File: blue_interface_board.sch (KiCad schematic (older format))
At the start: 0 parts

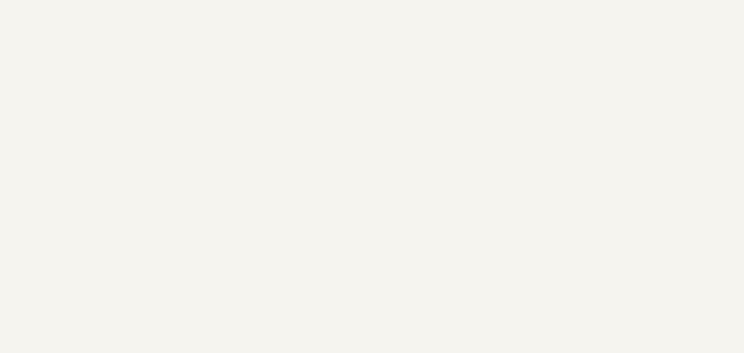
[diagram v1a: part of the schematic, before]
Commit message: Finished schematic, placement and routing, only silkscreen TODO
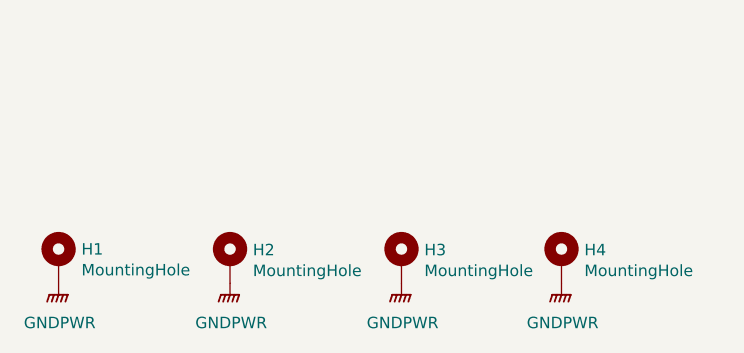
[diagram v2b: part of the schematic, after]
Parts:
- added H1, H2, H3, H4: MountingHole, MountingHole:MountingHole_2.5mm_Pad_Via, symbol Mechanical:MountingHole_Pad
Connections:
- new net GNDPWR: H1.1, H2.1, H3.1, H4.1
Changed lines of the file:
@@
 EESchema Schematic File Version 5
 LIBS:blue_interface_board-cache
-EELAYER 29 0
+EELAYER 30 0
 EELAYER END
 $Descr A4 11693 8268
@@
 F1 "Power.sch" 50
 $EndSheet
+$Comp
+L Mechanical:MountingHole_Pad H1
+U 1 1 5D50B183
+P 750 4250
+F 0 "H1" H 850 4299 50  0000 L CNN
+F 1 "MountingHole" H 850 4208 50  0000 L CNN
+F 2 "MountingHole:MountingHole_2.5mm_Pad_Via" H 750 4250 50  0001 C CNN
+F 3 "~" H 750 4250 50  0001 C CNN
+	1    750  4250
+	1    0    0    -1
+$EndComp
+$Comp
+L Mechanical:MountingHole_Pad H2
+U 1 1 5D50B77F
+P 1500 4250
+F 0 "H2" H 1600 4296 50  0000 L CNN
+F 1 "MountingHole" H 1600 4205 50  0000 L CNN
+F 2 "MountingHole:MountingHole_2.5mm_Pad_Via" H 1500 4250 50  0001 C CNN
+F 3 "~" H 1500 4250 50  0001 C CNN
+	1    1500 4250
+	1    0    0    -1
+$EndComp
+$Comp
+L Mechanical:MountingHole_Pad H3
+U 1 1 5D50B87B
+P 2250 4250
+F 0 "H3" H 2350 4296 50  0000 L CNN
+F 1 "MountingHole" H 2350 4205 50  0000 L CNN
+F 2 "MountingHole:MountingHole_2.5mm_Pad_Via" H 2250 4250 50  0001 C CNN
+F 3 "~" H 2250 4250 50  0001 C CNN
+	1    2250 4250
+	1    0    0    -1
+$EndComp
+$Comp
+L Mechanical:MountingHole_Pad H4
+U 1 1 5D50BAA4
+P 2950 4250
+F 0 "H4" H 3050 4296 50  0000 L CNN
+F 1 "MountingHole" H 3050 4205 50  0000 L CNN
+F 2 "MountingHole:MountingHole_2.5mm_Pad_Via" H 2950 4250 50  0001 C CNN
+F 3 "~" H 2950 4250 50  0001 C CNN
+	1    2950 4250
+	1    0    0    -1
+$EndComp
+$Comp
+L power:GNDPWR #PWR?
+U 1 1 5D51731A
+P 750 4350
+F 0 "#PWR?" H 750 4100 50  0001 C CNN
+F 1 "GNDPWR" H 755 4177 50  0000 C CNN
+F 2 "" H 750 4350 50  0001 C CNN
+F 3 "" H 750 4350 50  0001 C CNN
+	1    750  4350
+	1    0    0    -1
+$EndComp
+$Comp
+L power:GNDPWR #PWR?
+U 1 1 5D517AC5
+P 1500 4350
+F 0 "#PWR?" H 1500 4100 50  0001 C CNN
+F 1 "GNDPWR" H 1505 4177 50  0000 C CNN
+F 2 "" H 1500 4350 50  0001 C CNN
+F 3 "" H 1500 4350 50  0001 C CNN
+	1    1500 4350
+	1    0    0    -1
+$EndComp
+$Comp
+L power:GNDPWR #PWR?
+U 1 1 5D517D46
+P 2250 4350
+F 0 "#PWR?" H 2250 4100 50  0001 C CNN
+F 1 "GNDPWR" H 2255 4177 50  0000 C CNN
+F 2 "" H 2250 4350 50  0001 C CNN
+F 3 "" H 2250 4350 50  0001 C CNN
+	1    2250 4350
+	1    0    0    -1
+$EndComp
+$Comp
+L power:GNDPWR #PWR?
+U 1 1 5D518361
+P 2950 4350
+F 0 "#PWR?" H 2950 4100 50  0001 C CNN
+F 1 "GNDPWR" H 2955 4177 50  0000 C CNN
+F 2 "" H 2950 4350 50  0001 C CNN
+F 3 "" H 2950 4350 50  0001 C CNN
+	1    2950 4350
+	1    0    0    -1
+$EndComp
 $EndSCHEMATC

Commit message: Fix DRCs and minor improvements
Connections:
- net GNDPWR: no longer H3.1
- no-connect marks 0 -> 1
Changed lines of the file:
@@
 EESchema Schematic File Version 5
-LIBS:blue_interface_board-cache
 EELAYER 30 0
 EELAYER END
@@
 Comment3 ""
 Comment4 ""
+Comment5 ""
+Comment6 ""
+Comment7 ""
+Comment8 ""
+Comment9 ""
 $EndDescr
 $Sheet
@@
 $EndComp
 $Comp
-L power:GNDPWR #PWR?
+L power:GNDPWR #PWR0146
 U 1 1 5D51731A
 P 750 4350
-F 0 "#PWR?" H 750 4100 50  0001 C CNN
+F 0 "#PWR0146" H 750 4100 50  0001 C CNN
 F 1 "GNDPWR" H 755 4177 50  0000 C CNN
 F 2 "" H 750 4350 50  0001 C CNN
@@
 $EndComp
 $Comp
-L power:GNDPWR #PWR?
+L power:GNDPWR #PWR0149
 U 1 1 5D517AC5
 P 1500 4350
-F 0 "#PWR?" H 1500 4100 50  0001 C CNN
+F 0 "#PWR0149" H 1500 4100 50  0001 C CNN
 F 1 "GNDPWR" H 1505 4177 50  0000 C CNN
 F 2 "" H 1500 4350 50  0001 C CNN
@@
 $EndComp
 $Comp
-L power:GNDPWR #PWR?
-U 1 1 5D517D46
-P 2250 4350
-F 0 "#PWR?" H 2250 4100 50  0001 C CNN
-F 1 "GNDPWR" H 2255 4177 50  0000 C CNN
-F 2 "" H 2250 4350 50  0001 C CNN
-F 3 "" H 2250 4350 50  0001 C CNN
-	1    2250 4350
-	1    0    0    -1
-$EndComp
-$Comp
-L power:GNDPWR #PWR?
+L power:GNDPWR #PWR0155
 U 1 1 5D518361
 P 2950 4350
-F 0 "#PWR?" H 2950 4100 50  0001 C CNN
+F 0 "#PWR0155" H 2950 4100 50  0001 C CNN
 F 1 "GNDPWR" H 2955 4177 50  0000 C CNN
 F 2 "" H 2950 4350 50  0001 C CNN
@@
 	1    0    0    -1
 $EndComp
+NoConn ~ 2250 4350
 $EndSCHEMATC

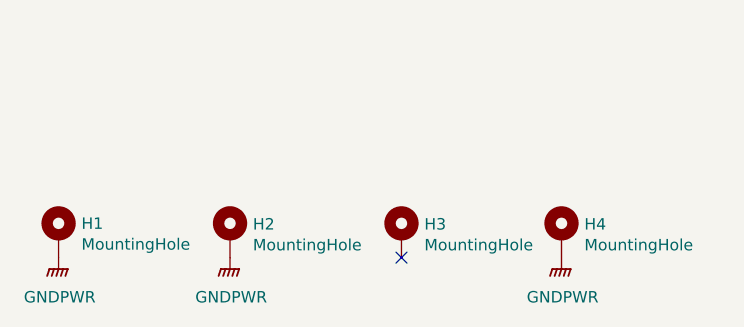
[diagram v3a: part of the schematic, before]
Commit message: Changed USB connector to be on same side
Signed-off-by: Luca Della Vedova <luca@openrobotics.org>
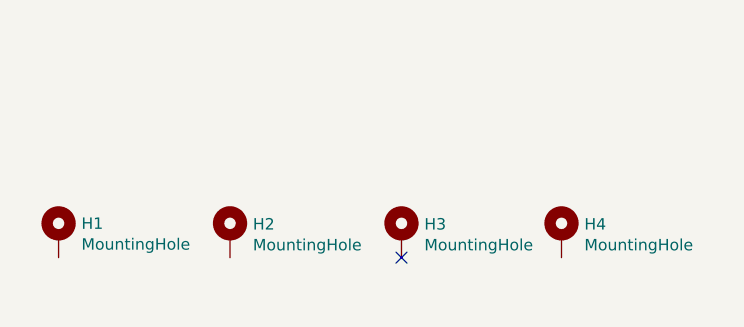
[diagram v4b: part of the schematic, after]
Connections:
- removed net GNDPWR: H1.1, H2.1, H4.1
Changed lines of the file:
@@
-	1    0    0    -1
-$EndComp
-$Comp
-L power:GNDPWR #PWR0146
-U 1 1 5D51731A
-P 750 4350
-F 0 "#PWR0146" H 750 4100 50  0001 C CNN
-F 1 "GNDPWR" H 755 4177 50  0000 C CNN
-F 2 "" H 750 4350 50  0001 C CNN
-F 3 "" H 750 4350 50  0001 C CNN
-	1    750  4350
-	1    0    0    -1
-$EndComp
-$Comp
-L power:GNDPWR #PWR0149
-U 1 1 5D517AC5
-P 1500 4350
-F 0 "#PWR0149" H 1500 4100 50  0001 C CNN
-F 1 "GNDPWR" H 1505 4177 50  0000 C CNN
-F 2 "" H 1500 4350 50  0001 C CNN
-F 3 "" H 1500 4350 50  0001 C CNN
-	1    1500 4350
-	1    0    0    -1
-$EndComp
-$Comp
-L power:GNDPWR #PWR0155
-U 1 1 5D518361
-P 2950 4350
-F 0 "#PWR0155" H 2950 4100 50  0001 C CNN
-F 1 "GNDPWR" H 2955 4177 50  0000 C CNN
-F 2 "" H 2950 4350 50  0001 C CNN
-F 3 "" H 2950 4350 50  0001 C CNN
-	1    2950 4350
 	1    0    0    -1
 $EndComp

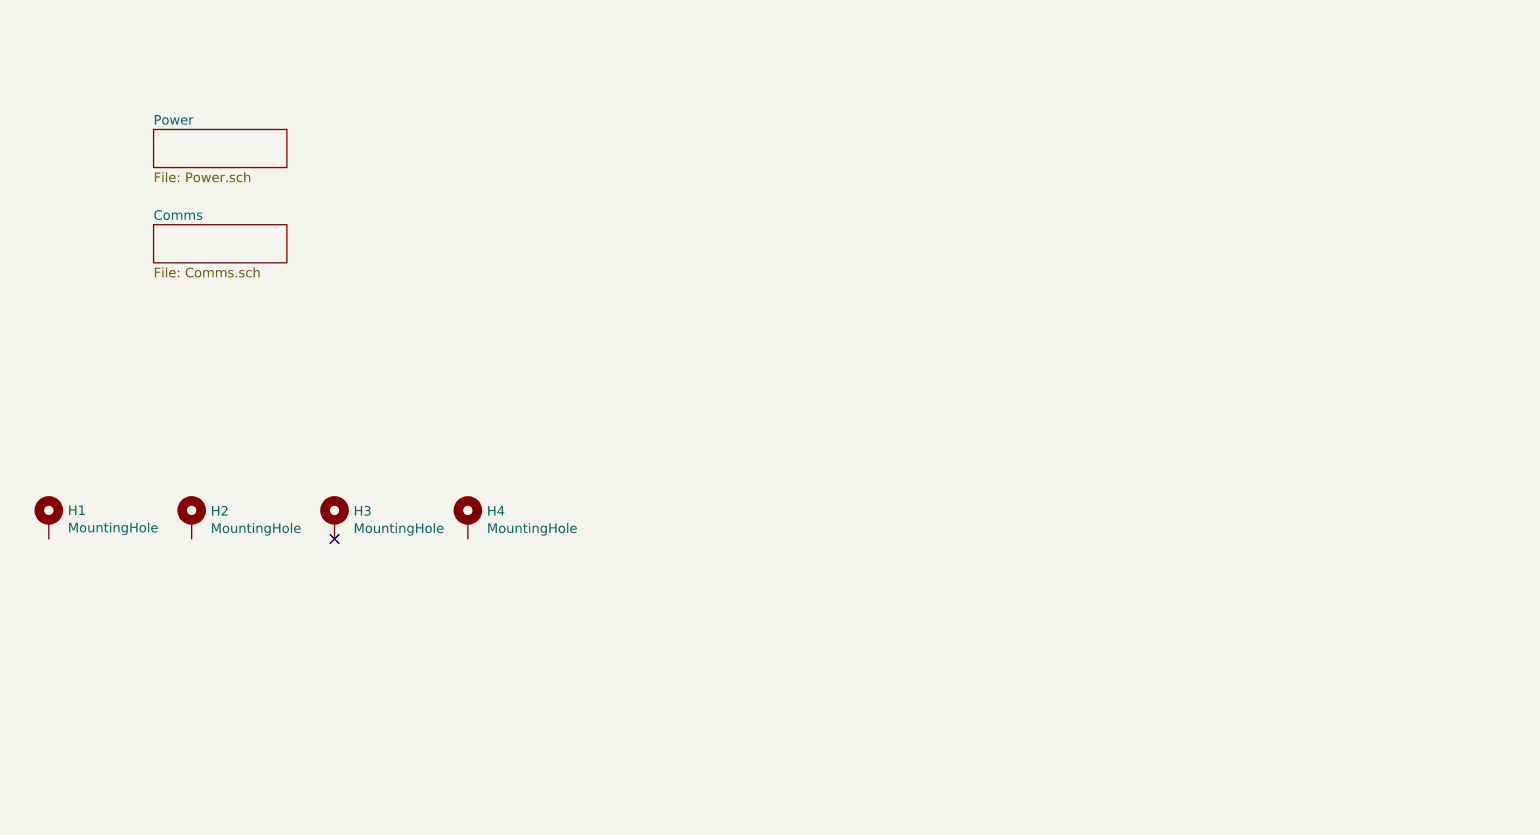
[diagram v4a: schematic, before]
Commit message: add rs485 termination, change to SOT-323 TVS diodes, various OCD
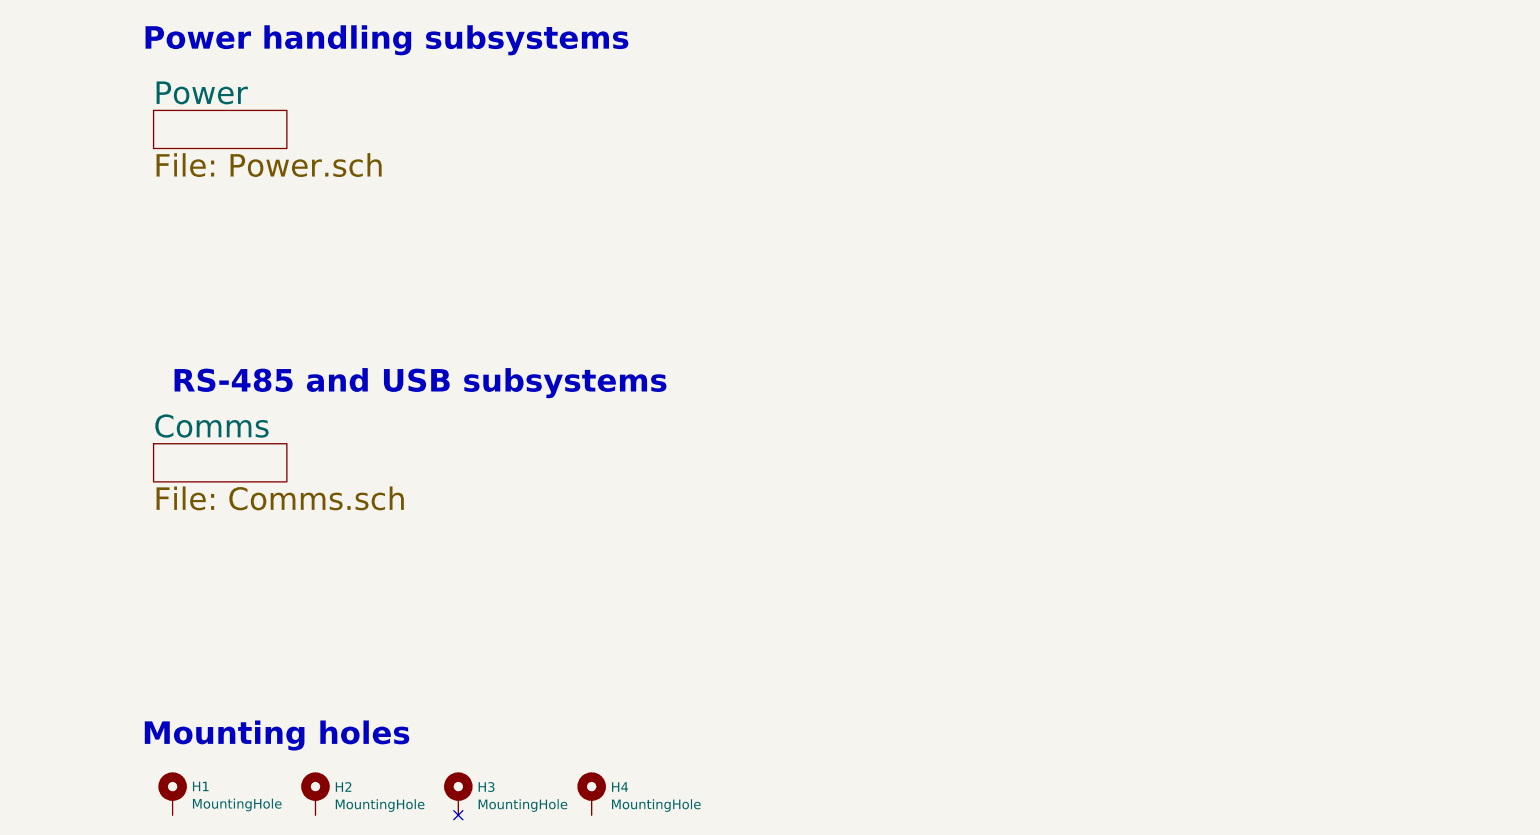
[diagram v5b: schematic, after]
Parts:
- H1, H2, H3, H4: footprint MountingHole:MountingHole_2.5mm_Pad_Via -> MountingHole:MountingHole_3.2mm_M3_DIN965_Pad
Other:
- note added: "Mounting holes"
- note added: "Power handling subsystems"
- note added: "RS-485 and USB subsystems"
- moved on the sheet: H1, H2, H3, H4
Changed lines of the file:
@@
 Comment9 ""
 $EndDescr
-$Sheet
-S 1300 2700 700  200
-U 5D27A619
-F0 "Comms" 50
-F1 "Comms.sch" 50
-$EndSheet
-$Sheet
-S 1300 2200 700  200
-U 5D2C77D8
-F0 "Power" 50
-F1 "Power.sch" 50
-$EndSheet
+NoConn ~ 2900 5800
+Text Notes 2650 5450 2    118  ~ 24
+Mounting holes
+Text Notes 3800 1800 2    118  ~ 24
+Power handling subsystems
+Text Notes 4000 3600 2    118  ~ 24
+RS-485 and USB subsystems
 $Comp
 L Mechanical:MountingHole_Pad H1
 U 1 1 5D50B183
-P 750 4250
-F 0 "H1" H 850 4299 50  0000 L CNN
-F 1 "MountingHole" H 850 4208 50  0000 L CNN
-F 2 "MountingHole:MountingHole_2.5mm_Pad_Via" H 750 4250 50  0001 C CNN
-F 3 "~" H 750 4250 50  0001 C CNN
-	1    750  4250
+P 1400 5700
+F 0 "H1" H 1500 5749 50  0000 L CNN
+F 1 "MountingHole" H 1500 5658 50  0000 L CNN
+F 2 "MountingHole:MountingHole_3.2mm_M3_DIN965_Pad" H 1400 5700 50  0001 C CNN
+F 3 "~" H 1400 5700 50  0001 C CNN
+	1    1400 5700
 	1    0    0    -1
 $EndComp
@@
 L Mechanical:MountingHole_Pad H2
 U 1 1 5D50B77F
-P 1500 4250
-F 0 "H2" H 1600 4296 50  0000 L CNN
-F 1 "MountingHole" H 1600 4205 50  0000 L CNN
-F 2 "MountingHole:MountingHole_2.5mm_Pad_Via" H 1500 4250 50  0001 C CNN
-F 3 "~" H 1500 4250 50  0001 C CNN
-	1    1500 4250
+P 2150 5700
+F 0 "H2" H 2250 5746 50  0000 L CNN
+F 1 "MountingHole" H 2250 5655 50  0000 L CNN
+F 2 "MountingHole:MountingHole_3.2mm_M3_DIN965_Pad" H 2150 5700 50  0001 C CNN
+F 3 "~" H 2150 5700 50  0001 C CNN
+	1    2150 5700
 	1    0    0    -1
 $EndComp
@@
 L Mechanical:MountingHole_Pad H3
 U 1 1 5D50B87B
-P 2250 4250
-F 0 "H3" H 2350 4296 50  0000 L CNN
-F 1 "MountingHole" H 2350 4205 50  0000 L CNN
-F 2 "MountingHole:MountingHole_2.5mm_Pad_Via" H 2250 4250 50  0001 C CNN
-F 3 "~" H 2250 4250 50  0001 C CNN
-	1    2250 4250
+P 2900 5700
+F 0 "H3" H 3000 5746 50  0000 L CNN
+F 1 "MountingHole" H 3000 5655 50  0000 L CNN
+F 2 "MountingHole:MountingHole_3.2mm_M3_DIN965_Pad" H 2900 5700 50  0001 C CNN
+F 3 "~" H 2900 5700 50  0001 C CNN
+	1    2900 5700
 	1    0    0    -1
 $EndComp
@@
 L Mechanical:MountingHole_Pad H4
 U 1 1 5D50BAA4
-P 2950 4250
-F 0 "H4" H 3050 4296 50  0000 L CNN
-F 1 "MountingHole" H 3050 4205 50  0000 L CNN
-F 2 "MountingHole:MountingHole_2.5mm_Pad_Via" H 2950 4250 50  0001 C CNN
-F 3 "~" H 2950 4250 50  0001 C CNN
-	1    2950 4250
+P 3600 5700
+F 0 "H4" H 3700 5746 50  0000 L CNN
+F 1 "MountingHole" H 3700 5655 50  0000 L CNN
+F 2 "MountingHole:MountingHole_3.2mm_M3_DIN965_Pad" H 3600 5700 50  0001 C CNN
+F 3 "~" H 3600 5700 50  0001 C CNN
+	1    3600 5700
 	1    0    0    -1
 $EndComp
-NoConn ~ 2250 4350
+$Sheet
+S 1300 3850 700  200
+U 5D27A619
+F0 "Comms" 118
+F1 "Comms.sch" 118
+$EndSheet
+$Sheet
+S 1300 2100 700  200
+U 5D2C77D8
+F0 "Power" 118
+F1 "Power.sch" 118
+$EndSheet
 $EndSCHEMATC

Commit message: working through the power subsystems now. changed e-stop topology.
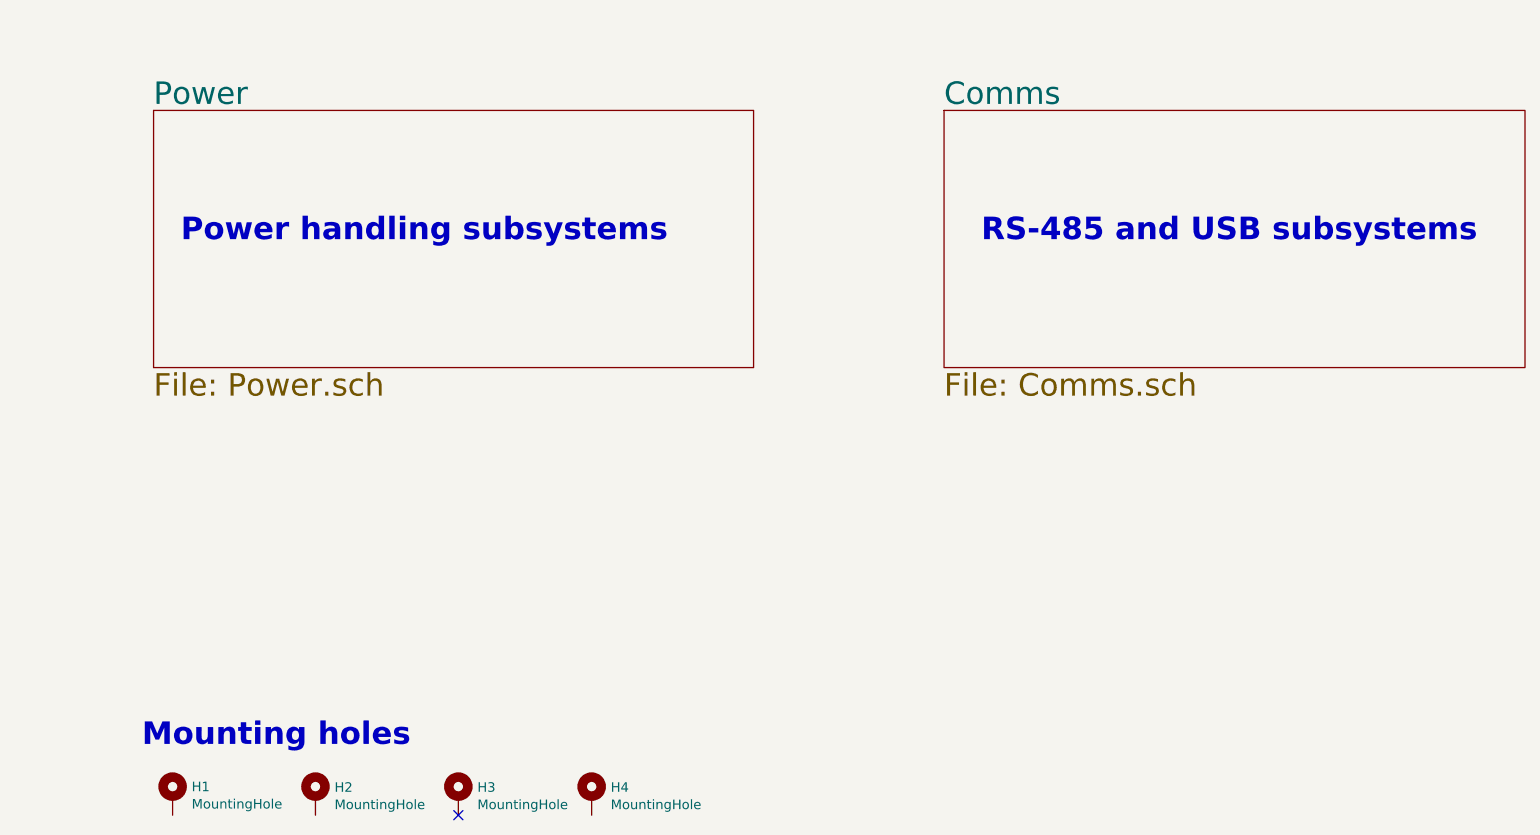
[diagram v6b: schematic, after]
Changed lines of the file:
@@
 Text Notes 2650 5450 2    118  ~ 24
 Mounting holes
-Text Notes 3800 1800 2    118  ~ 24
+Text Notes 4000 2800 2    118  ~ 24
 Power handling subsystems
-Text Notes 4000 3600 2    118  ~ 24
+Text Notes 8250 2800 2    118  ~ 24
 RS-485 and USB subsystems
 $Comp
@@
 $EndComp
 $Sheet
-S 1300 3850 700  200
+S 5450 2100 3050 1350
 U 5D27A619
 F0 "Comms" 118
@@
 $EndSheet
 $Sheet
-S 1300 2100 700  200
+S 1300 2100 3150 1350
 U 5D2C77D8
 F0 "Power" 118
